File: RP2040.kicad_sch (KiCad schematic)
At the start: 24 parts, among them J1 Conn_01x02, U3 W25Q128JVSI, U4 RP2040, Y1 ABM8-272-T3

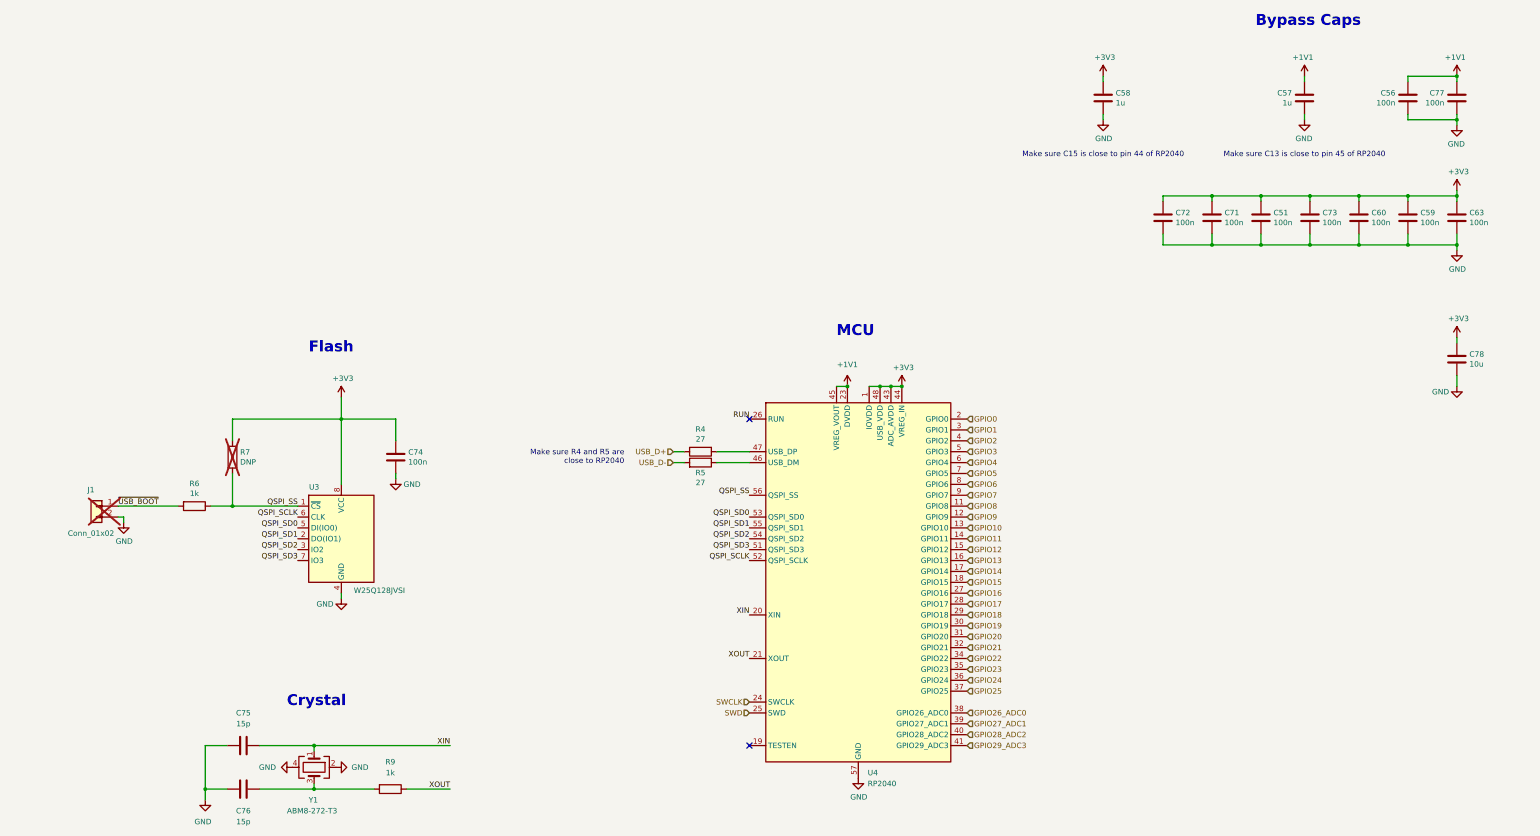
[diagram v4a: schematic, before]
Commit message: bulk cap and level shifter (still need to lay out)
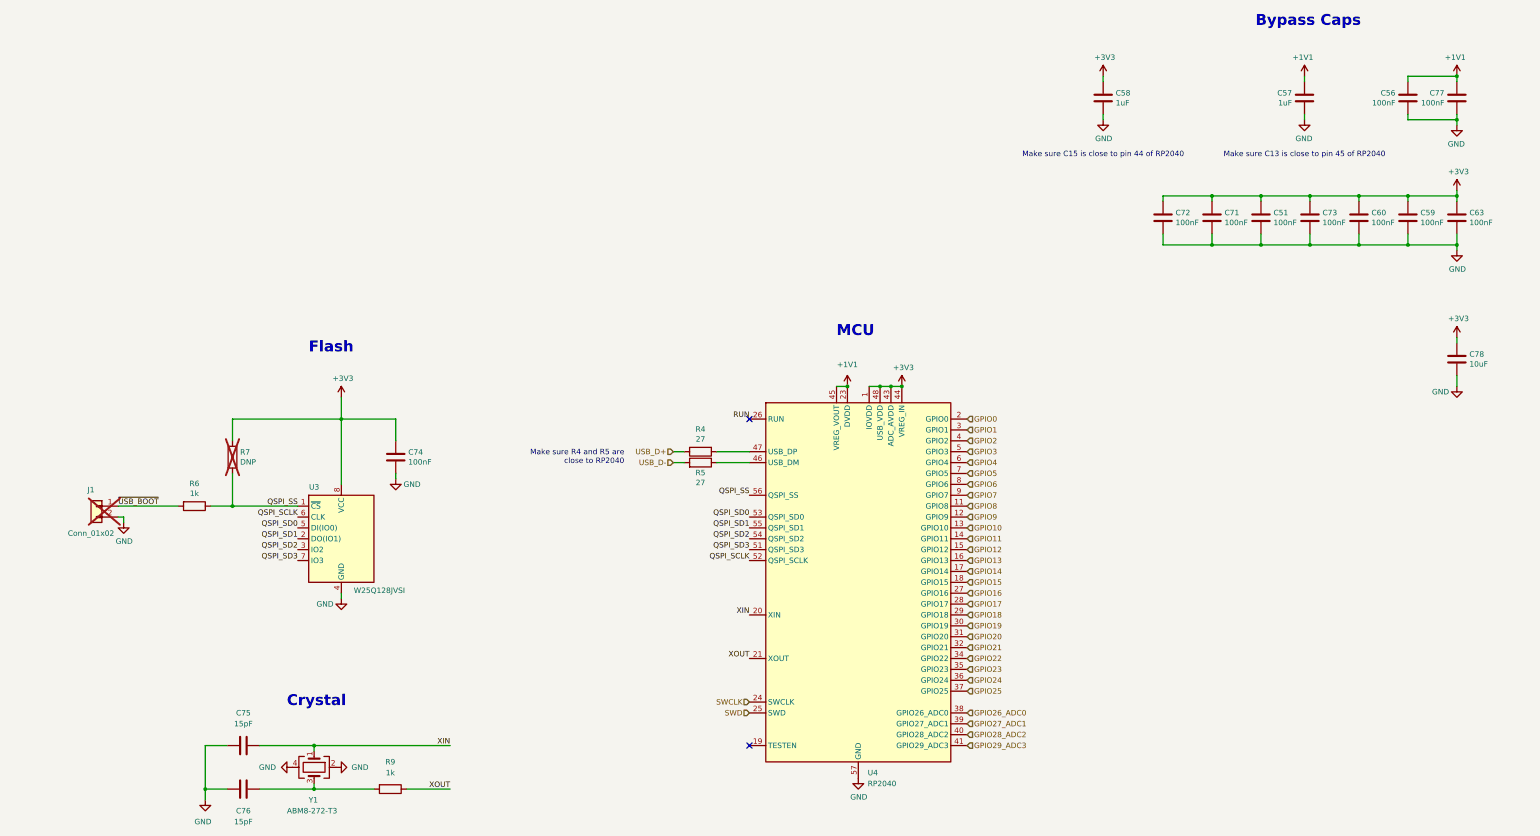
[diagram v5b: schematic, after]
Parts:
- C51, C56, C59, C60, C63, C71, C72, C73, C74, C77: value 100n -> 100nF; Manufacturer Samsung Electro-Mechanics -> Samsung Electro-Mechanics
- C57, C58: value 1u -> 1uF; LCSC C14445 -> C52923; MPN CL05A105KP5NNNC -> CL05A105KA5NQNC; Manufacturer Samsung Electro-Mechanics -> Samsung Electro-Mechanics
- C75, C76: value 15p -> 15pF; LCSC C86285 -> C1548; MPN CL05C150JB5NNNC -> 0402CG150J500NT; Manufacturer Samsung Electro-Mechanics -> FH (Guangdong Fenghua Advanced Tech)
- C78: value 10u -> 10uF
- J1, R7: MPN (none) -> DNP
- R4, R5: LCSC C25156 -> C25765; MPN 0402WGJ0270TCE -> 0402WGF2002TCE
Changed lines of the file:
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@@
 			)
 		)
-		(property "Value" "15p"
+		(property "Value" "15pF"
 			(at 97.79 212.09 90)
 			(effects
@@
 			)
 		)
-		(property "LCSC" "C86285"
+		(property "LCSC" "C1548"
 			(at 97.79 204.47 0)
 			(effects
@@
 			)
 		)
-		(property "MPN" "CL05C150JB5NNNC"
+		(property "MPN" "0402CG150J500NT"
 			(at 97.79 204.47 0)
 			(effects
@@
 			)
 		)
-		(property "Manufacturer" "Samsung Electro-Mechanics "
+		(property "Manufacturer" " FH (Guangdong Fenghua Advanced Tech)"
 			(at 97.79 204.47 0)
 			(effects
@@
 			)
 		)
-		(property "Value" "100n"
+		(property "Value" "100nF"
 			(at 372.491 72.263 0)
 			(effects
@@
 			)
 		)
-		(property "Manufacturer" "Samsung Electro-Mechanics "
+		(property "Manufacturer" "Samsung Electro-Mechanics"
 			(at 369.57 71.12 0)
 			(effects
@@
 			)
 		)
-		(property "Value" "100n"
+		(property "Value" "100nF"
 			(at 326.771 72.263 0)
 			(effects
@@
 			)
 		)
-		(property "Manufacturer" "Samsung Electro-Mechanics "
+		(property "Manufacturer" "Samsung Electro-Mechanics"
 			(at 323.85 71.12 0)
 			(effects
@@
 			)
 		)
-		(property "Value" "10u"
+		(property "Value" "10uF"
 			(at 383.921 105.283 0)
 			(effects
@@
 			)
 		)
-		(property "Value" "100n"
+		(property "Value" "100nF"
 			(at 361.061 72.263 0)
 			(effects
@@
 			)
 		)
-		(property "Manufacturer" "Samsung Electro-Mechanics "
+		(property "Manufacturer" "Samsung Electro-Mechanics"
 			(at 358.14 71.12 0)
 			(effects
@@
 			)
 		)
-		(property "Value" "100n"
+		(property "Value" "100nF"
 			(at 315.341 72.263 0)
 			(effects
@@
 			)
 		)
-		(property "Manufacturer" "Samsung Electro-Mechanics "
+		(property "Manufacturer" "Samsung Electro-Mechanics"
 			(at 312.42 71.12 0)
 			(effects
@@
 			)
 		)
-		(property "Value" "100n"
+		(property "Value" "100nF"
 			(at 378.079 44.323 0)
 			(effects
@@
 			)
 		)
-		(property "Manufacturer" "Samsung Electro-Mechanics "
+		(property "Manufacturer" "Samsung Electro-Mechanics"
 			(at 381 43.18 0)
 			(effects
@@
 			)
 		)
-		(property "Value" "1u"
+		(property "Value" "1uF"
 			(at 342.519 44.323 0)
 			(effects
@@
 			)
 		)
-		(property "LCSC" "C14445"
+		(property "LCSC" "C52923"
 			(at 345.44 43.18 0)
 			(effects
@@
 			)
 		)
-		(property "MPN" "CL05A105KP5NNNC"
+		(property "MPN" "CL05A105KA5NQNC"
 			(at 345.44 43.18 0)
 			(effects
@@
 			)
 		)
-		(property "Manufacturer" " Samsung Electro-Mechanics "
+		(property "Manufacturer" " Samsung Electro-Mechanics"
 			(at 345.44 43.18 0)
 			(effects
@@
 			)
 		)
-		(property "Value" "100n"
+		(property "Value" "100nF"
 			(at 349.631 72.263 0)
 			(effects
@@
 			)
 		)
-		(property "Manufacturer" "Samsung Electro-Mechanics "
+		(property "Manufacturer" "Samsung Electro-Mechanics"
 			(at 346.71 71.12 0)
 			(effects
@@
 			)
 		)
-		(property "Value" "100n"
+		(property "Value" "100nF"
 			(at 366.649 44.323 0)
 			(effects
@@
 			)
 		)
-		(property "Manufacturer" "Samsung Electro-Mechanics "
+		(property "Manufacturer" "Samsung Electro-Mechanics"
 			(at 369.57 43.18 0)
 			(effects
@@
 			)
 		)
-		(property "Value" "1u"
+		(property "Value" "1uF"
 			(at 301.371 44.323 0)
 			(effects
@@
 			)
 		)
-		(property "LCSC" "C14445"
+		(property "LCSC" "C52923"
 			(at 298.45 43.18 0)
 			(effects
@@
 			)
 		)
-		(property "MPN" "CL05A105KP5NNNC"
+		(property "MPN" "CL05A105KA5NQNC"
 			(at 298.45 43.18 0)
 			(effects
@@
 			)
 		)
-		(property "Manufacturer" " Samsung Electro-Mechanics "
+		(property "Manufacturer" " Samsung Electro-Mechanics"
 			(at 298.45 43.18 0)
 			(effects
@@
 			)
 		)
-		(property "Value" "100n"
+		(property "Value" "100nF"
 			(at 338.201 72.263 0)
 			(effects
@@
 			)
 		)
-		(property "Manufacturer" "Samsung Electro-Mechanics "
+		(property "Manufacturer" "Samsung Electro-Mechanics"
 			(at 335.28 71.12 0)
 			(effects
@@
 			)
 		)
-		(property "Value" "100n"
+		(property "Value" "100nF"
 			(at 136.271 128.143 0)
 			(effects
@@
 			)
 		)
-		(property "Manufacturer" "Samsung Electro-Mechanics "
+		(property "Manufacturer" "Samsung Electro-Mechanics"
 			(at 133.35 127 0)
 			(effects
@@
 			)
 		)
-		(property "MPN" ""
+		(property "MPN" "DNP"
 			(at 63.5 138.43 0)
 			(effects
@@
 			)
 		)
-		(property "Value" "15p"
+		(property "Value" "15pF"
 			(at 97.79 189.23 90)
 			(effects
@@
 			)
 		)
-		(property "LCSC" "C86285"
+		(property "LCSC" "C1548"
 			(at 97.79 194.31 0)
 			(effects
@@
 			)
 		)
-		(property "MPN" "CL05C150JB5NNNC"
+		(property "MPN" "0402CG150J500NT"
 			(at 97.79 194.31 0)
 			(effects
@@
 			)
 		)
-		(property "Manufacturer" "Samsung Electro-Mechanics "
+		(property "Manufacturer" " FH (Guangdong Fenghua Advanced Tech)"
 			(at 97.79 194.31 0)
 			(effects
@@
 			)
 		)
-		(property "Value" "100n"
+		(property "Value" "100nF"
 			(at 383.921 72.263 0)
 			(effects
@@
 			)
 		)
-		(property "Manufacturer" "Samsung Electro-Mechanics "
+		(property "Manufacturer" "Samsung Electro-Mechanics"
 			(at 381 71.12 0)
 			(effects
@@
 			)
 		)
-		(property "LCSC" "C25156"
+		(property "LCSC" "C25765"
 			(at 204.47 128.27 0)
 			(effects
@@
 			)
 		)
-		(property "MPN" " 0402WGJ0270TCE"
+		(property "MPN" "0402WGF2002TCE"
 			(at 204.47 128.27 0)
 			(effects
@@
 			)
 		)
-		(property "MPN" ""
+		(property "MPN" "DNP"
 			(at 95.25 127 0)
 			(effects
@@
 			)
 		)
-		(property "LCSC" "C25156"
+		(property "LCSC" "C25765"
 			(at 204.47 125.73 0)
 			(effects
@@
 			)
 		)
-		(property "MPN" " 0402WGJ0270TCE"
+		(property "MPN" "0402WGF2002TCE"
 			(at 204.47 125.73 0)
 			(effects

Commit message: add debug led, make bulk caps smaller, export plate and bottom for rudimentary case
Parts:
- C57, C58: Manufacturer Samsung Electro-Mechanics -> Samsung Electro-Mechanics
- C75, C76: Manufacturer FH (Guangdong Fenghua Advanced Tech) -> FH (Guangdong Fenghua Advanced Tech)
- R4, R5: LCSC C25765 -> C25100; MPN 0402WGF2002TCE -> 0402WGF270JTCE
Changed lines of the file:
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@@
 			)
 		)
-		(property "Manufacturer" " FH (Guangdong Fenghua Advanced Tech)"
+		(property "Manufacturer" "FH (Guangdong Fenghua Advanced Tech)"
 			(at 97.79 204.47 0)
 			(effects
@@
 			)
 		)
-		(property "Manufacturer" " Samsung Electro-Mechanics"
+		(property "Manufacturer" "Samsung Electro-Mechanics"
 			(at 345.44 43.18 0)
 			(effects
@@
 			)
 		)
-		(property "Manufacturer" " Samsung Electro-Mechanics"
+		(property "Manufacturer" "Samsung Electro-Mechanics"
 			(at 298.45 43.18 0)
 			(effects
@@
 			)
 		)
-		(property "Manufacturer" " FH (Guangdong Fenghua Advanced Tech)"
+		(property "Manufacturer" "FH (Guangdong Fenghua Advanced Tech)"
 			(at 97.79 194.31 0)
 			(effects
@@
 			)
 		)
-		(property "LCSC" "C25765"
+		(property "LCSC" "C25100"
 			(at 204.47 128.27 0)
 			(effects
@@
 			)
 		)
-		(property "MPN" "0402WGF2002TCE"
+		(property "MPN" "0402WGF270JTCE"
 			(at 204.47 128.27 0)
 			(effects
@@
 			)
 		)
-		(property "LCSC" "C25765"
+		(property "LCSC" "C25100"
 			(at 204.47 125.73 0)
 			(effects
@@
 			)
 		)
-		(property "MPN" "0402WGF2002TCE"
+		(property "MPN" "0402WGF270JTCE"
 			(at 204.47 125.73 0)
 			(effects

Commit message: fab output changes (part choice updates)
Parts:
- J1: Type DNS -> THT
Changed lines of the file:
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@@
 			)
 		)
-		(property "Type" "DNS"
+		(property "Type" "THT"
 			(at 63.5 138.43 0)
 			(effects
